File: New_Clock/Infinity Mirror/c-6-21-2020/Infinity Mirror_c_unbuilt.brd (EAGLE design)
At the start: 81 x 26 mm, 19 parts, among them IC1 MSGEQ7P, J1 Vsupply, J2 AUDIO_POTS, J3 LED, U1 DS1307, Y1 32.768kHz

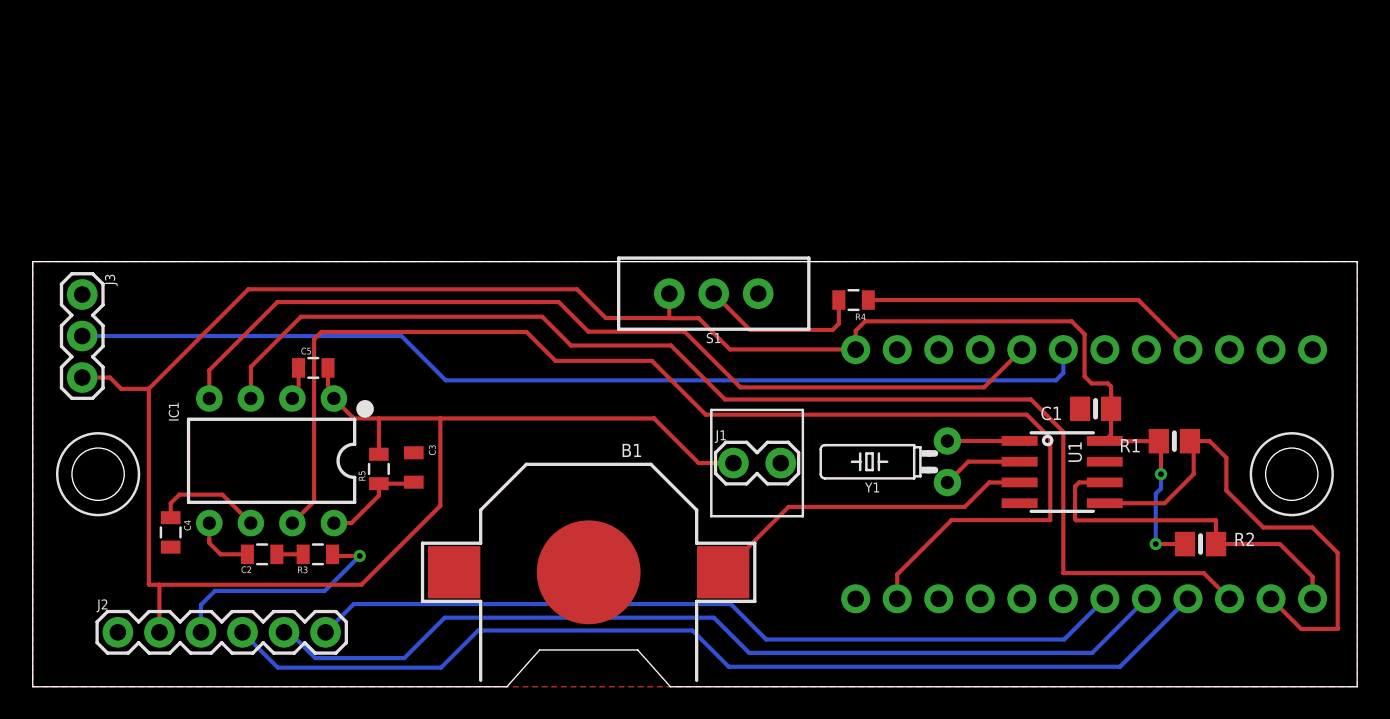
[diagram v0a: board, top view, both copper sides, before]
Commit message: created rec v with a larger board with integrated 8 throw switches. found 3D models and ported circuit box for editing in Fusion. NOTE: THIS CAD IS NOT EXACTLY THE SAME AS THE REAL CLOCK
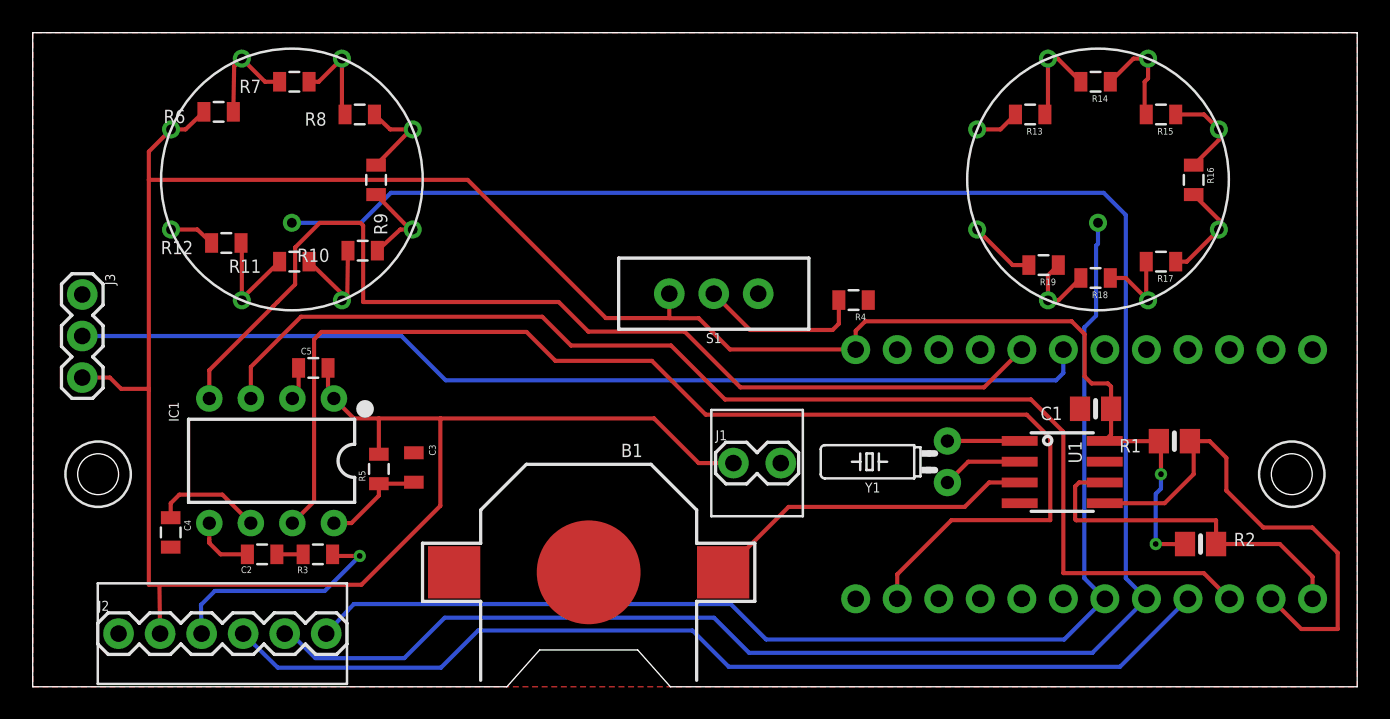
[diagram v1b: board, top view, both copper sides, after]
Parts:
- added R10, R11, R12, R13, R14, R15, R16, R17, R18, R19, R6, R7, R8, R9: 10K, RC1a_Main_2-20-2018_m:SPARKFUN-PASSIVES_0805
- added U$2, U$3: ROTARY-SWITCH-8POS, _111_IH:ROTARY-SWITCH-8POS
- moved J2 0.09 mm to (5.25, 3.25)
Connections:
- new net N$1: R8.1, R9.1, U$2.4
- new net N$12: R16.2, R17.1, U$3.5
- new net N$13: R17.2, R18.1, U$3.6
- new net N$14: R18.2, R19.1, U$3.7
- new net N$15: R19.2, U$3.GND
- new net N$17: R13.1, R14.2, U$3.2
- new net N$18: R14.1, R15.2, U$3.3
- new net N$19: R15.1, R16.1, U$3.4
- new net N$2: R7.1, R8.2, U$2.3
- new net N$3: R6.1, R7.2, U$2.2
- new net N$5: R12.2, U$2.GND
- new net N$6: R11.2, R12.1, U$2.7
- new net N$7: R10.2, R11.1, U$2.6
- new net N$9: R10.1, R9.2, U$2.5
- net POT_1: now also U$3.VOUT
- net POT_2: now also U$2.VOUT
- net VCC: now also R13.2, R6.2, U$2.VIN, U$3.VIN
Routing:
- net POT_2: track 56.7 -> 133.0 mm
- net POT_1: track 50.3 -> 74.2 mm
- net VCC: track 158.3 -> 180.7 mm
- net ~3: track 20.8 -> 0.00 mm
- net 4-STROBE: track 56.3 -> 64.3 mm
- net N$6: track 0.00 -> 6.86 mm
- net N$18: track 0.00 -> 6.44 mm
- net N$7: track 0.00 -> 6.39 mm
- net N$3: track 0.00 -> 6.35 mm
- net N$12: track 0.00 -> 6.23 mm
- net N$2: track 0.00 -> 6.11 mm
- net N$17: track 0.00 -> 6.09 mm
- net N$19: track 0.00 -> 5.84 mm
- net N$9: track 0.00 -> 5.81 mm
- net N$1: track 0.00 -> 5.71 mm
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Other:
- board size 81 x 26 mm -> 81 x 40 mm
